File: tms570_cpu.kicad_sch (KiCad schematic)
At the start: 49 parts, among them J12 TSW-103-08-F-S-RA, J3 FTSH-105-01-L-DV-K, U2 TMS570LS0914APGEQQ1

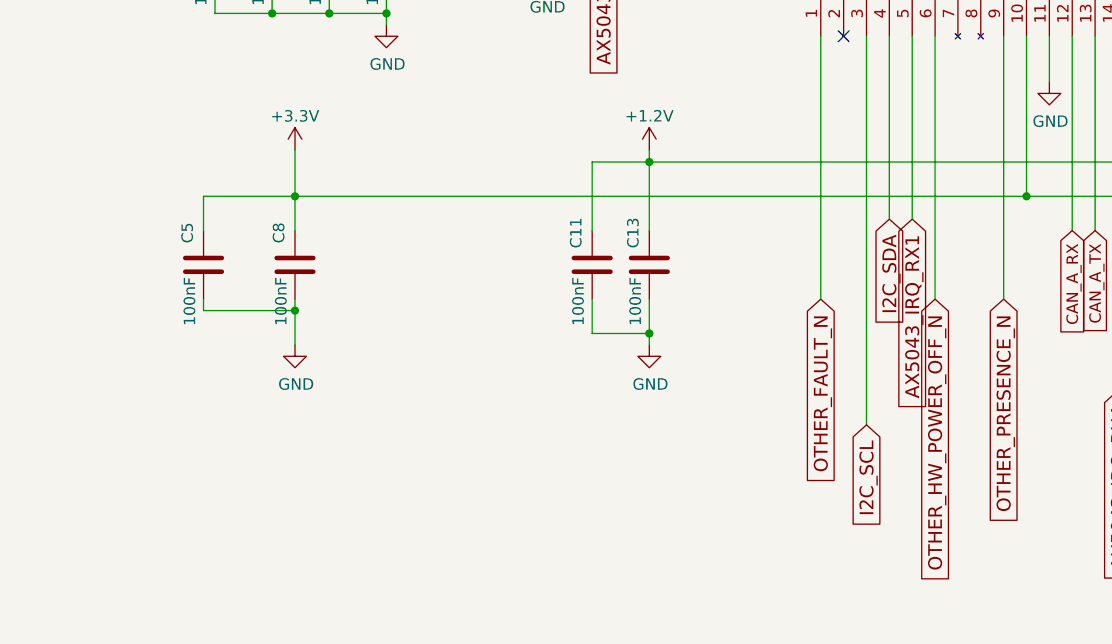
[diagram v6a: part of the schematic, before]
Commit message: Fix latch up or pull down issues with the active/standby lines
There are either latch-up or pull-down issues when the processor is
powered off.  Make a bunch of the active/standby lines controlled
by MOSFETs to avoid this issue.

Signed-off-by: Corey Minyard <corey@minyard.net>
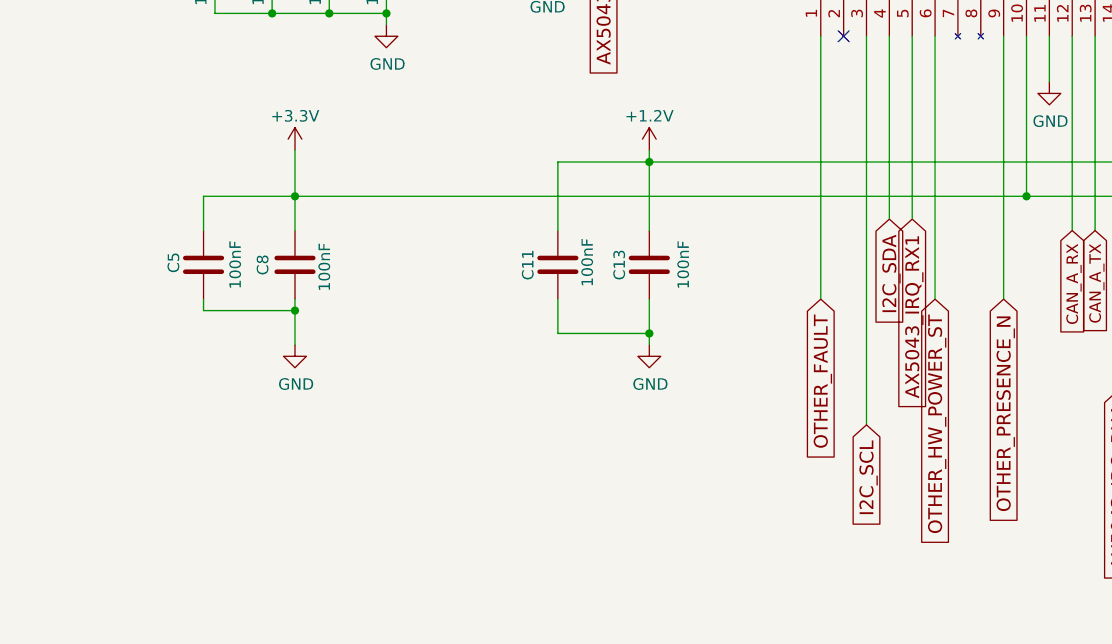
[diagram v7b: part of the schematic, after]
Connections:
- net OTHER_FAULT_N renamed OTHER_FAULT
- net OTHER_HW_POWER_OFF_N renamed OTHER_HW_POWER_ST
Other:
- moved on the sheet: C11
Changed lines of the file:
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@@
 	(wire
 		(pts
-			(xy 146.05 226.06) (xy 146.05 218.44)
+			(xy 142.24 226.06) (xy 142.24 218.44)
 		)
 		(stroke
@@
 	(wire
 		(pts
-			(xy 146.05 218.44) (xy 152.4 218.44)
+			(xy 142.24 218.44) (xy 152.4 218.44)
 		)
 		(stroke
@@
 	(wire
 		(pts
-			(xy 146.05 237.49) (xy 152.4 237.49)
+			(xy 142.24 237.49) (xy 152.4 237.49)
 		)
 		(stroke
@@
 	(wire
 		(pts
-			(xy 146.05 233.68) (xy 146.05 237.49)
+			(xy 142.24 233.68) (xy 142.24 237.49)
 		)
 		(stroke
@@
 		)
 	)
-	(global_label "OTHER_HW_POWER_OFF_N"
+	(global_label "OTHER_HW_POWER_ST"
 		(shape input)
 		(at 184.15 233.68 270)
@@
 		)
 		(property "Intersheetrefs" "${INTERSHEET_REFS}"
-			(at 184.15 265.2877 90)
+			(at 184.15 260.9333 90)
 			(effects
 				(font
@@
 		)
 	)
-	(global_label "OTHER_FAULT_N"
+	(global_label "OTHER_FAULT"
 		(shape input)
 		(at 171.45 233.68 270)
@@
 		)
 		(property "Intersheetrefs" "${INTERSHEET_REFS}"
-			(at 171.45 254.2568 90)
+			(at 171.45 251.4991 90)
 			(effects
 				(font
@@
 		(dnp no)
 		(property "Reference" "C8"
-			(at 111.252 226.314 90)
+			(at 109.474 229.87 90)
 			(effects
 				(font
@@
 		)
 		(property "Value" "100nF"
-			(at 111.506 233.934 90)
+			(at 116.332 230.124 90)
 			(effects
 				(font
@@
 		(dnp no)
 		(property "Reference" "C13"
-			(at 150.622 226.314 90)
+			(at 149.098 229.87 90)
 			(effects
 				(font
@@
 		)
 		(property "Value" "100nF"
-			(at 150.876 233.934 90)
+			(at 156.21 229.87 90)
 			(effects
 				(font
@@
 		(dnp no)
 		(property "Reference" "C5"
-			(at 101.092 226.314 90)
+			(at 99.568 229.616 90)
 			(effects
 				(font
@@
 		)
 		(property "Value" "100nF"
-			(at 101.346 233.934 90)
+			(at 106.426 229.87 90)
 			(effects
 				(font
@@
 	(symbol
 		(lib_id "Device:C")
-		(at 146.05 229.87 0)
+		(at 142.24 229.87 0)
 		(unit 1)
 		(exclude_from_sim no)
@@
 		(dnp no)
 		(property "Reference" "C11"
-			(at 144.272 226.314 90)
+			(at 138.938 229.87 90)
 			(effects
 				(font
@@
 		)
 		(property "Value" "100nF"
-			(at 144.526 233.934 90)
+			(at 145.542 229.616 90)
 			(effects
 				(font
@@
 		)
 		(property "Footprint" "Capacitor_SMD:C_0402_1005Metric_Pad0.74x0.62mm_HandSolder"
-			(at 147.0152 233.68 0)
+			(at 143.2052 233.68 0)
 			(effects
 				(font
@@
 		)
 		(property "Datasheet" "~"
-			(at 146.05 229.87 0)
+			(at 142.24 229.87 0)
 			(effects
 				(font
@@
 		)
 		(property "Description" ""
-			(at 146.05 229.87 0)
+			(at 142.24 229.87 0)
 			(effects
 				(font

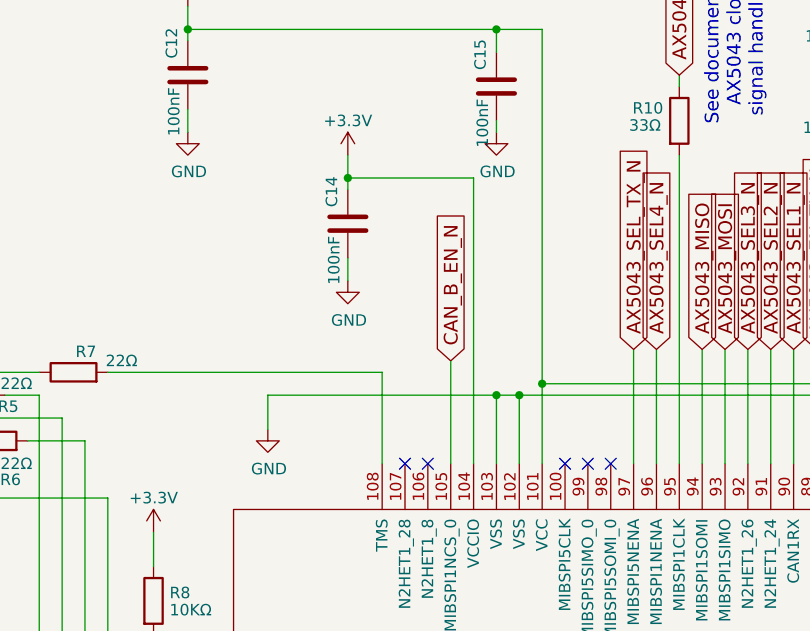
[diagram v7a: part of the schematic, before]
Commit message: Add a DAC to the PA Iref input
Allow the power the PA uses to be directly controlled.

Signed-off-by: Corey Minyard <corey@minyard.net>
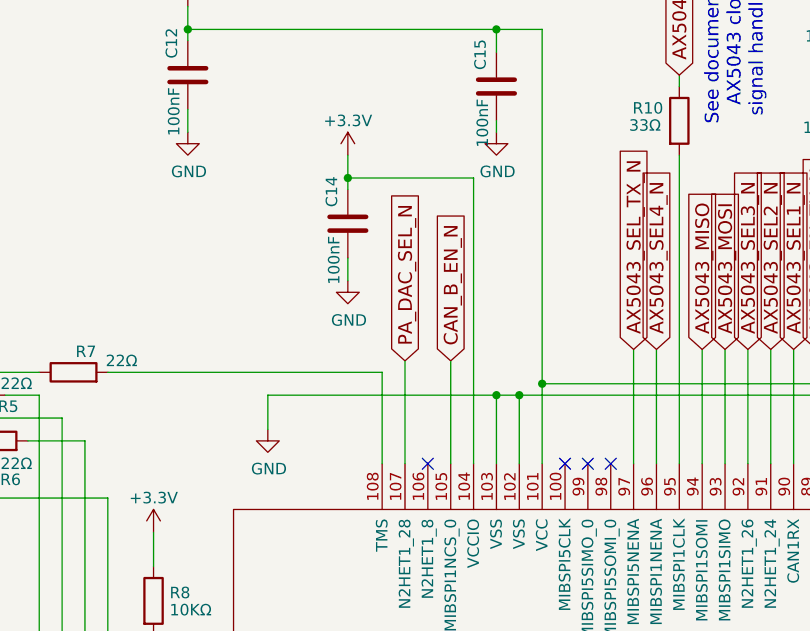
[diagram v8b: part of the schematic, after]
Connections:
- net PA_DAC_SEL_N: now reaches U2.107 (N2HET1_28)
- no-connect marks 18 -> 17
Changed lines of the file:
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@@
 	)
 	(no_connect
-		(at 173.99 72.39)
-	)
-	(no_connect
 		(at 250.19 204.47)
 	)
@@
 		)
 	)
+	(wire
+		(pts
+			(xy 173.99 60.96) (xy 173.99 72.39)
+		)
+		(stroke
+			(width 0)
+			(type default)
+		)
+	)
 	(global_label "AX5043_EN_RX1_N"
 		(shape input)
@@
 			(effects
 				(font
+					(size 1.27 1.27)
+				)
+				(justify left)
+				(hide yes)
+			)
+		)
+	)
+	(global_label "PA_DAC_SEL_N"
+		(shape input)
+		(at 173.99 60.96 90)
+		(fields_autoplaced yes)
+		(effects
+			(font
+				(size 1.524 1.524)
+			)
+			(justify left)
+		)
+		(property "Intersheetrefs" "${INTERSHEET_REFS}"
+			(at 173.99 41.8347 90)
+			(effects
+				(font
